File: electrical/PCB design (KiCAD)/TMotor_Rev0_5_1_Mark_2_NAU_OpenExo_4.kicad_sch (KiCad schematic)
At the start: 2 parts

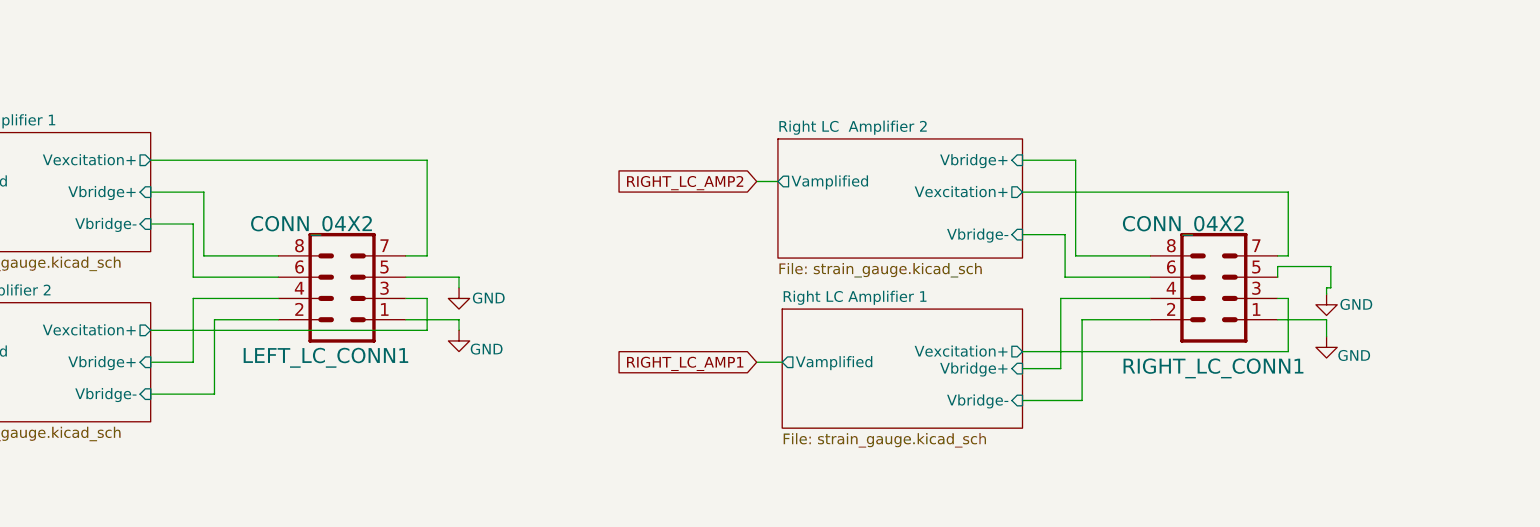
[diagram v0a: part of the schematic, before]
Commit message: Updated KiCAD for next iteration (some minor fixes) ; functional Servo controller and MIT is working over serial
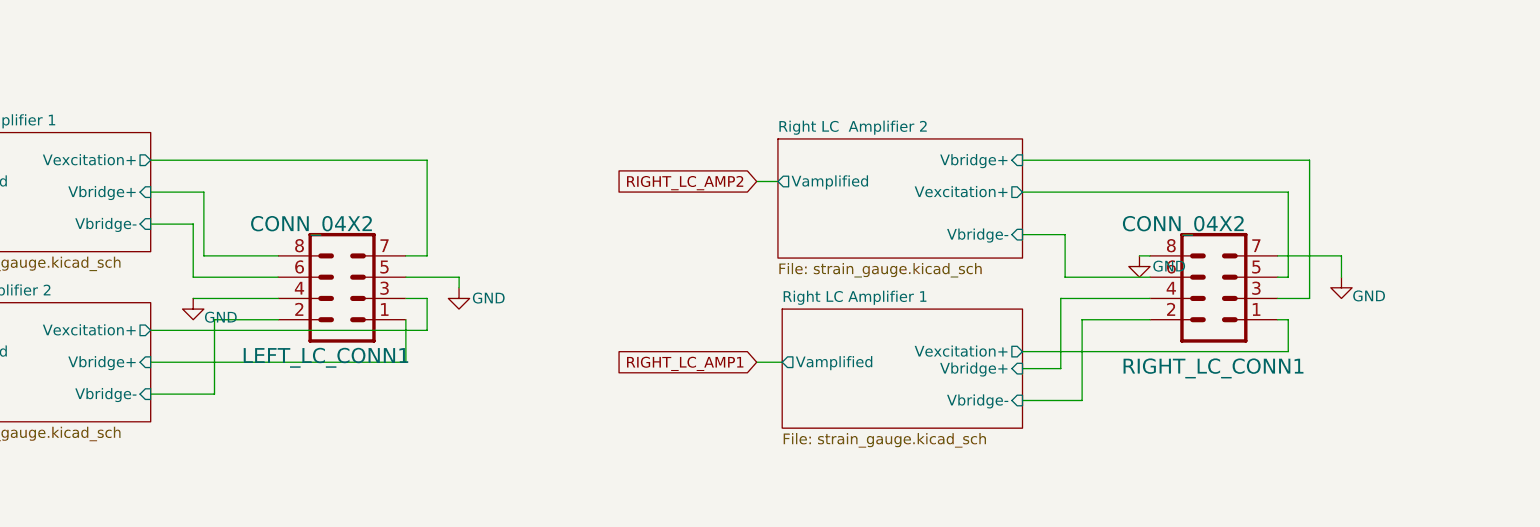
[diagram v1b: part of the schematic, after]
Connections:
- net GND: now also LEFT_LC_CONN1.4, RIGHT_LC_CONN1.7, RIGHT_LC_CONN1.8; no longer LEFT_LC_CONN1.1, RIGHT_LC_CONN1.1, RIGHT_LC_CONN1.5
- net Left LC Amplifier 2/Vbridge+: now also LEFT_LC_CONN1.1; no longer LEFT_LC_CONN1.4
- net Right LC  Amplifier 2/Vbridge+: now also RIGHT_LC_CONN1.3; no longer RIGHT_LC_CONN1.8
- net Right LC  Amplifier 2/Vexcitation+: now also RIGHT_LC_CONN1.5; no longer RIGHT_LC_CONN1.7
- net Right LC Amplifier 1/Vexcitation+: now also RIGHT_LC_CONN1.1; no longer RIGHT_LC_CONN1.3
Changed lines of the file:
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@@
 	(wire
 		(pts
-			(xy 222.25 96.52) (xy 228.092 96.52)
-		)
-		(stroke
-			(width 0)
-			(type default)
-		)
-	)
-	(wire
-		(pts
-			(xy 198.12 88.9) (xy 207.01 88.9)
+			(xy 229.87 88.9) (xy 229.87 91.44)
+		)
+		(stroke
+			(width 0)
+			(type default)
+		)
+	)
+	(wire
+		(pts
+			(xy 118.11 101.6) (xy 118.11 96.52)
 		)
 		(stroke
@@
 	(wire
 		(pts
-			(xy 191.77 77.47) (xy 198.12 77.47)
+			(xy 191.77 77.47) (xy 226.06 77.47)
 		)
 		(stroke
@@
 	(wire
 		(pts
-			(xy 228.6 90.17) (xy 228.6 92.71)
-		)
-		(stroke
-			(width 0)
-			(type default)
-		)
-	)
-	(wire
-		(pts
 			(xy 93.98 81.28) (xy 93.98 88.9)
 		)
@@
 	(wire
 		(pts
-			(xy 228.092 96.52) (xy 228.092 98.552)
-		)
-		(stroke
-			(width 0)
-			(type default)
-		)
-	)
-	(wire
-		(pts
-			(xy 228.6 92.71) (xy 228.092 92.71)
-		)
-		(stroke
-			(width 0)
-			(type default)
-		)
-	)
-	(wire
-		(pts
 			(xy 87.63 85.09) (xy 92.71 85.09)
 		)
@@
 	(wire
 		(pts
-			(xy 118.11 96.52) (xy 124.46 96.52)
+			(xy 205.74 88.9) (xy 207.01 88.9)
 		)
 		(stroke
@@
 	(wire
 		(pts
+			(xy 223.52 96.52) (xy 222.25 96.52)
+		)
+		(stroke
+			(width 0)
+			(type default)
+		)
+	)
+	(wire
+		(pts
 			(xy 191.77 106.172) (xy 198.882 106.172)
 		)
@@
 	(wire
 		(pts
-			(xy 92.71 93.98) (xy 92.71 101.6)
-		)
-		(stroke
-			(width 0)
-			(type default)
-		)
-	)
-	(wire
-		(pts
 			(xy 120.65 88.9) (xy 120.65 77.47)
 		)
@@
 	(wire
 		(pts
-			(xy 222.25 93.98) (xy 223.52 93.98)
+			(xy 92.71 93.98) (xy 102.87 93.98)
 		)
 		(stroke
@@
 	(wire
 		(pts
-			(xy 222.25 90.17) (xy 228.6 90.17)
-		)
-		(stroke
-			(width 0)
-			(type default)
-		)
-	)
-	(wire
-		(pts
 			(xy 120.65 93.98) (xy 120.65 97.79)
 		)
@@
 	(wire
 		(pts
+			(xy 223.52 91.44) (xy 222.25 91.44)
+		)
+		(stroke
+			(width 0)
+			(type default)
+		)
+	)
+	(wire
+		(pts
 			(xy 160.02 101.6) (xy 163.068 101.6)
 		)
@@
 	(wire
 		(pts
+			(xy 223.52 100.33) (xy 223.52 96.52)
+		)
+		(stroke
+			(width 0)
+			(type default)
+		)
+	)
+	(wire
+		(pts
+			(xy 226.06 77.47) (xy 226.06 93.98)
+		)
+		(stroke
+			(width 0)
+			(type default)
+		)
+	)
+	(wire
+		(pts
 			(xy 93.98 88.9) (xy 102.87 88.9)
 		)
@@
 	(wire
 		(pts
-			(xy 198.12 77.47) (xy 198.12 88.9)
-		)
-		(stroke
-			(width 0)
-			(type default)
-		)
-	)
-	(wire
-		(pts
-			(xy 102.87 93.98) (xy 92.71 93.98)
-		)
-		(stroke
-			(width 0)
-			(type default)
-		)
-	)
-	(wire
-		(pts
 			(xy 120.65 88.9) (xy 118.11 88.9)
 		)
@@
 	(wire
 		(pts
-			(xy 228.092 92.71) (xy 228.092 93.472)
+			(xy 223.52 81.28) (xy 223.52 91.44)
 		)
 		(stroke
@@
 	(wire
 		(pts
-			(xy 222.25 91.44) (xy 222.25 90.17)
-		)
-		(stroke
-			(width 0)
-			(type default)
-		)
-	)
-	(wire
-		(pts
-			(xy 223.52 88.9) (xy 223.52 81.28)
-		)
-		(stroke
-			(width 0)
-			(type default)
-		)
-	)
-	(wire
-		(pts
 			(xy 196.342 93.98) (xy 196.342 102.362)
 		)
@@
 	(wire
 		(pts
-			(xy 124.46 96.52) (xy 124.46 97.79)
+			(xy 226.06 93.98) (xy 222.25 93.98)
 		)
 		(stroke
@@
 	(wire
 		(pts
-			(xy 223.52 93.98) (xy 223.52 100.33)
-		)
-		(stroke
-			(width 0)
-			(type default)
-		)
-	)
-	(wire
-		(pts
 			(xy 191.77 100.33) (xy 223.52 100.33)
 		)
@@
 	(wire
 		(pts
-			(xy 92.71 101.6) (xy 87.63 101.6)
+			(xy 87.63 101.6) (xy 118.11 101.6)
 		)
 		(stroke
@@
 	(wire
 		(pts
-			(xy 222.25 88.9) (xy 223.52 88.9)
+			(xy 222.25 88.9) (xy 229.87 88.9)
 		)
 		(stroke
@@
 	(symbol
 		(lib_id "power:GND")
-		(at 228.092 93.472 0)
+		(at 205.74 88.9 0)
 		(unit 1)
 		(exclude_from_sim no)
@@
 		(dnp no)
 		(property "Reference" "#PWR018"
-			(at 228.092 99.822 0)
+			(at 205.74 95.25 0)
 			(effects
 				(font
@@
 		)
 		(property "Value" "GND"
-			(at 231.648 94.742 0)
+			(at 209.296 90.17 0)
 			(effects
 				(font
@@
 		)
 		(property "Footprint" ""
-			(at 228.092 93.472 0)
+			(at 205.74 88.9 0)
 			(effects
 				(font
@@
 		)
 		(property "Datasheet" ""
-			(at 228.092 93.472 0)
+			(at 205.74 88.9 0)
 			(effects
 				(font
@@
 		)
 		(property "Description" "Power symbol creates a global label with name \"GND\" , ground"
-			(at 228.092 93.472 0)
+			(at 205.74 88.9 0)
 			(effects
 				(font
@@
 	(symbol
 		(lib_id "power:GND")
-		(at 228.092 98.552 0)
+		(at 229.87 91.44 0)
 		(unit 1)
 		(exclude_from_sim no)
@@
 		(dnp no)
 		(property "Reference" "#PWR019"
-			(at 228.092 104.902 0)
+			(at 229.87 97.79 0)
 			(effects
 				(font
@@
 		)
 		(property "Value" "GND"
-			(at 231.394 100.838 0)
+			(at 233.172 93.726 0)
 			(effects
 				(font
@@
 		)
 		(property "Footprint" ""
-			(at 228.092 98.552 0)
+			(at 229.87 91.44 0)
 			(effects
 				(font
@@
 		)
 		(property "Datasheet" ""
-			(at 228.092 98.552 0)
+			(at 229.87 91.44 0)
 			(effects
 				(font
@@
 		)
 		(property "Description" "Power symbol creates a global label with name \"GND\" , ground"
-			(at 228.092 98.552 0)
+			(at 229.87 91.44 0)
 			(effects
 				(font
@@
 	(symbol
 		(lib_id "power:GND")
-		(at 124.46 97.79 0)
+		(at 92.71 93.98 0)
 		(unit 1)
 		(exclude_from_sim no)
@@
 		(dnp no)
 		(property "Reference" "#PWR013"
-			(at 124.46 104.14 0)
+			(at 92.71 100.33 0)
 			(effects
 				(font
@@
 		)
 		(property "Value" "GND"
-			(at 127.762 100.076 0)
+			(at 96.012 96.266 0)
 			(effects
 				(font
@@
 		)
 		(property "Footprint" ""
-			(at 124.46 97.79 0)
+			(at 92.71 93.98 0)
 			(effects
 				(font
@@
 		)
 		(property "Datasheet" ""
-			(at 124.46 97.79 0)
+			(at 92.71 93.98 0)
 			(effects
 				(font
@@
 		)
 		(property "Description" "Power symbol creates a global label with name \"GND\" , ground"
-			(at 124.46 97.79 0)
-			(effects
-				(font
+			(at 92.71 93.98 0)
+			(effects
+				(font
